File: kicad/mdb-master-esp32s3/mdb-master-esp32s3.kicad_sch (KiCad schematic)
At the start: 39 parts, among them J1 Conn_02x11_Odd_Even, J2 USB_C_Receptacle_USB2.0_16P, J3 MDB_Connector, J4 Barrel_Jack, Q1 BC807, SW1 SW_Push, U1 ESP32-S3FH4R2, U2 LM2594HVM-3.3, Y1 Crystal_GND24

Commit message: Exclude from BOM
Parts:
- C2: now left out of the parts list
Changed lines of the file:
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@@
 		(unit 1)
 		(exclude_from_sim no)
-		(in_bom yes)
+		(in_bom no)
 		(on_board yes)
 		(dnp no)

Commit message: Refacting
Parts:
- added TP2: TestPoint, TestPoint:TestPoint_Pad_D1.0mm, symbol Connector:TestPoint
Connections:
- net vin: now also TP2.1
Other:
- moved on the sheet: TP1
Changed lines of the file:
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@@
 	)
 	(junction
+		(at 518.16 212.09)
+		(diameter 0)
+		(color 0 0 0 0)
+	)
+	(junction
 		(at 100.33 146.05)
 		(diameter 0)
@@
 	(wire
 		(pts
-			(xy 516.89 212.09) (xy 511.81 212.09)
+			(xy 523.24 212.09) (xy 518.16 212.09)
 		)
 		(stroke
@@
 	(wire
 		(pts
-			(xy 274.32 55.88) (xy 276.86 55.88)
+			(xy 518.16 212.09) (xy 511.81 212.09)
 		)
 		(stroke
@@
 	(wire
 		(pts
-			(xy 95.25 153.67) (xy 95.25 156.21)
+			(xy 274.32 55.88) (xy 276.86 55.88)
 		)
 		(stroke
@@
 	(wire
 		(pts
-			(xy 92.71 60.96) (xy 92.71 59.69)
+			(xy 95.25 153.67) (xy 95.25 156.21)
 		)
 		(stroke
@@
 	)
 	(symbol
+		(lib_id "Connector:TestPoint")
+		(at 450.85 209.55 0)
+		(unit 1)
+		(exclude_from_sim no)
+		(in_bom yes)
+		(on_board yes)
+		(dnp no)
+		(fields_autoplaced yes)
+		(property "Reference" "TP2"
+			(at 453.39 204.9779 0)
+			(effects
+				(font
+					(size 1.27 1.27)
+				)
+				(justify left)
+			)
+		)
+		(property "Value" "TestPoint"
+			(at 453.39 207.5179 0)
+			(effects
+				(font
+					(size 1.27 1.27)
+				)
+				(justify left)
+			)
+		)
+		(property "Footprint" "TestPoint:TestPoint_Pad_D1.0mm"
+			(at 455.93 209.55 0)
+			(effects
+				(font
+					(size 1.27 1.27)
+				)
+				(hide yes)
+			)
+		)
+		(property "Datasheet" "~"
+			(at 455.93 209.55 0)
+			(effects
+				(font
+					(size 1.27 1.27)
+				)
+				(hide yes)
+			)
+		)
+		(property "Description" "test point"
+			(at 450.85 209.55 0)
+			(effects
+				(font
+					(size 1.27 1.27)
+				)
+				(hide yes)
+			)
+		)
+		(pin "1"
+		)
+		(instances
+			(project "mdb-master-esp32s3"
+				(path "/1a9a25ce-6784-46e5-b680-57f383f3a43d"
+					(reference "TP2")
+					(unit 1)
+				)
+			)
+		)
+	)
+	(symbol
 		(lib_id "Device:C")
 		(at 201.93 59.69 180)
@@
 	(symbol
 		(lib_id "Connector:TestPoint")
-		(at 92.71 59.69 0)
+		(at 518.16 212.09 0)
 		(unit 1)
 		(exclude_from_sim no)
@@
 		(fields_autoplaced yes)
 		(property "Reference" "TP1"
-			(at 95.25 55.1179 0)
+			(at 520.7 207.5179 0)
 			(effects
 				(font
@@
 		)
 		(property "Value" "TestPoint"
-			(at 95.25 57.6579 0)
+			(at 520.7 210.0579 0)
 			(effects
 				(font
@@
 		)
 		(property "Footprint" "TestPoint:TestPoint_Pad_D1.0mm"
-			(at 97.79 59.69 0)
+			(at 523.24 212.09 0)
 			(effects
 				(font
@@
 		)
 		(property "Datasheet" "~"
-			(at 97.79 59.69 0)
+			(at 523.24 212.09 0)
 			(effects
 				(font
@@
 		)
 		(property "Description" "test point"
-			(at 92.71 59.69 0)
+			(at 518.16 212.09 0)
 			(effects
 				(font
@@
 	(symbol
 		(lib_id "power:+3V3")
-		(at 516.89 212.09 270)
+		(at 523.24 212.09 270)
 		(unit 1)
 		(exclude_from_sim no)
@@
 		(fields_autoplaced yes)
 		(property "Reference" "#PWR043"
-			(at 513.08 212.09 0)
+			(at 519.43 212.09 0)
 			(effects
 				(font
@@
 		)
 		(property "Value" "+3V3"
-			(at 520.7 212.0899 90)
+			(at 527.05 212.0899 90)
 			(effects
 				(font
@@
 		)
 		(property "Footprint" ""
-			(at 516.89 212.09 0)
+			(at 523.24 212.09 0)
 			(effects
 				(font
@@
 		)
 		(property "Datasheet" ""
-			(at 516.89 212.09 0)
+			(at 523.24 212.09 0)
 			(effects
 				(font
@@
 		)
 		(property "Description" ""
-			(at 516.89 212.09 0)
+			(at 523.24 212.09 0)
 			(effects
 				(font
@@
 					(unit 1)
 				)
-			)
-		)
-	)
-	(symbol
-		(lib_id "power:+3V3")
-		(at 92.71 60.96 180)
-		(unit 1)
-		(exclude_from_sim no)
-		(in_bom yes)
-		(on_board yes)
-		(dnp no)
-		(fields_autoplaced yes)
-		(property "Reference" "#PWR07"
-			(at 92.71 57.15 0)
-			(effects
-				(font
-					(size 1.27 1.27)
-				)
-				(hide yes)
-			)
-		)
-		(property "Value" "+3V3"
-			(at 92.71 66.04 0)
-			(effects
-				(font
-					(size 1.27 1.27)
-				)
-			)
-		)
-		(property "Footprint" ""
-			(at 92.71 60.96 0)
-			(effects
-				(font
-					(size 1.27 1.27)
-				)
-				(hide yes)
-			)
-		)
-		(property "Datasheet" ""
-			(at 92.71 60.96 0)
-			(effects
-				(font
-					(size 1.27 1.27)
-				)
-				(hide yes)
-			)
-		)
-		(property "Description" ""
-			(at 92.71 60.96 0)
-			(effects
-				(font
-					(size 1.27 1.27)
-				)
-				(hide yes)
-			)
-		)
-		(pin "1"
-		)
-		(instances
-			(project "mdb-master-esp32s3"
-				(path "/1a9a25ce-6784-46e5-b680-57f383f3a43d"
-					(reference "#PWR07")
-					(unit 1)
-				)

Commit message: Master initial routing
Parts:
- removed AE1: Antenna, RF_Antenna:Texas_SWRA117D_2.4GHz_Left, symbol Device:Antenna
- removed C1: 1.8pf, Capacitor_SMD:C_0603_1608Metric, symbol Device:C
- removed C2: NC, Capacitor_SMD:C_0603_1608Metric, symbol Device:C
- removed L1: 2.4nh, Inductor_SMD:L_0603_1608Metric, symbol Device:L
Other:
- moved on the sheet: C10, C11, C12, C13, C3, C4, C5, C6, C7, C8, C9, D1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

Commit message: Refacting production components
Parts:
- J3: LCSC# (none) -> C22365701
- J4: LCSC# (none) -> C7498153
- Q1: LCSC# (none) -> C57316
- R7, R9: LCSC# (none) -> C2907113
- R8: LCSC# (none) -> C23162
- TP1, TP2: now left out of the parts list
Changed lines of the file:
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@@
 			)
 		)
+		(property "LCSC#" "C57316"
+			(at 356.87 128.27 0)
+			(effects
+				(font
+					(size 1.27 1.27)
+				)
+				(hide yes)
+			)
+		)
 		(pin "3"
 		)
@@
 			)
 		)
+		(property "LCSC#" "C2907113"
+			(at 325.12 92.71 0)
+			(effects
+				(font
+					(size 1.27 1.27)
+				)
+				(hide yes)
+			)
+		)
 		(pin "2"
 		)
@@
 			)
 		)
+		(property "LCSC#" "C2907113"
+			(at 359.41 113.03 0)
+			(effects
+				(font
+					(size 1.27 1.27)
+				)
+				(hide yes)
+			)
+		)
 		(pin "2"
 		)
@@
 		(unit 1)
 		(exclude_from_sim no)
-		(in_bom yes)
+		(in_bom no)
 		(on_board yes)
 		(dnp no)
@@
 		(unit 1)
 		(exclude_from_sim no)
-		(in_bom yes)
+		(in_bom no)
 		(on_board yes)
 		(dnp no)
@@
 			)
 		)
+		(property "LCSC#" "C22365701"
+			(at 340.36 66.04 0)
+			(effects
+				(font
+					(size 1.27 1.27)
+				)
+				(hide yes)
+			)
+		)
 		(pin "2"
 		)
@@
 			)
 		)
+		(property "LCSC#" "C23162"
+			(at 347.98 128.27 90)
+			(effects
+				(font
+					(size 1.27 1.27)
+				)
+				(hide yes)
+			)
+		)
 		(pin "2"
 		)
@@
 			(at 379.73 214.63 0)
 			(effects
+				(font
+					(size 1.27 1.27)
+				)
+				(hide yes)
+			)
+		)
+		(property "LCSC#" "C7498153"
+			(at 379.73 214.63 0)
+			(effects

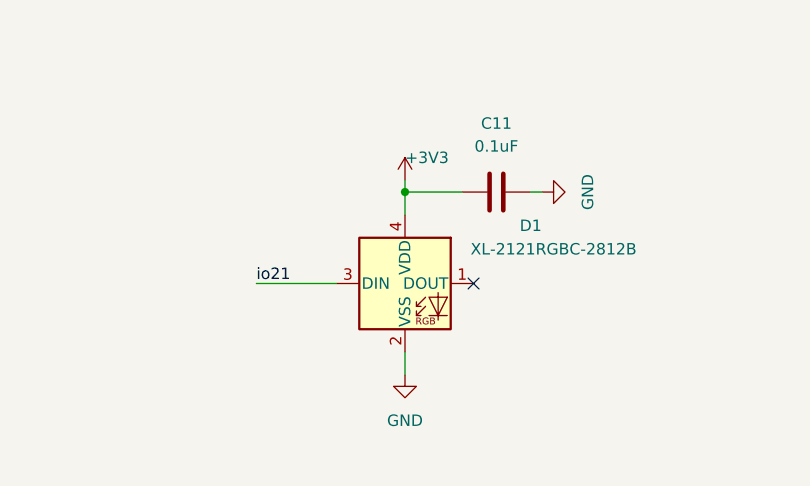
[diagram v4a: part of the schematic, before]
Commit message: Updating LED footprint
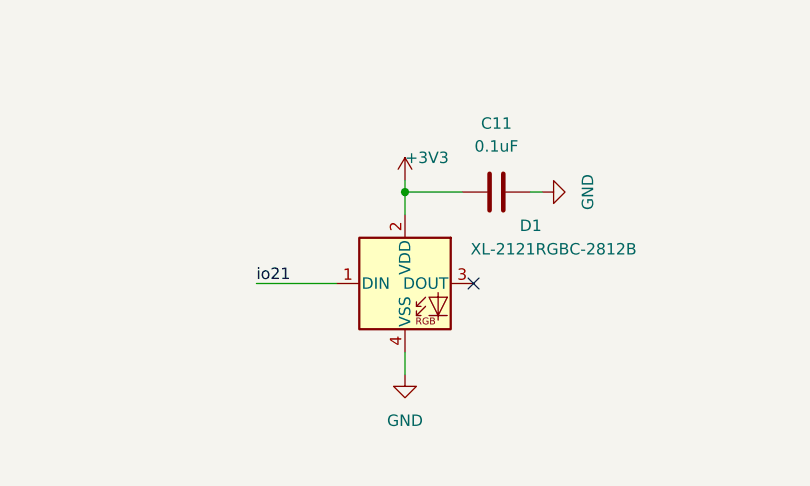
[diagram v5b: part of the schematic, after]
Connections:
- net +3V3: now also D1.2 (VDD); no longer D1.4 (VDD)
- net GND: now also D1.4 (VSS); no longer D1.2 (VSS)
- net io21: now also D1.1 (DIN); no longer D1.3 (DIN)
